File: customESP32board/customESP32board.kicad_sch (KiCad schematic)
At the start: 50 parts, among them J1 USB_B_Micro, J2 Conn_01x16_Pin, J3 Conn_01x16_Pin, Q1 S8050, Q2 S8050, Q3 BSS138, Q4 BSS138, Q5 BSS138, SW1 SW_Push, SW2 SW_Push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

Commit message: update pcb board size to 65mm x 60mm
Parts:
- J1: footprint Connector_USB:USB_Micro-B_Wuerth_629105150521 -> Connector_USB:USB_C_Receptacle_GCT_USB4125-xx-x-0190_6P_TopMnt_Horizontal
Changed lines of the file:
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@@
 			)
 		)
-		(property "Footprint" "Connector_USB:USB_Micro-B_Wuerth_629105150521"
+		(property "Footprint" "Connector_USB:USB_C_Receptacle_GCT_USB4125-xx-x-0190_6P_TopMnt_Horizontal"
 			(at 25.4 41.91 0)
 			(effects

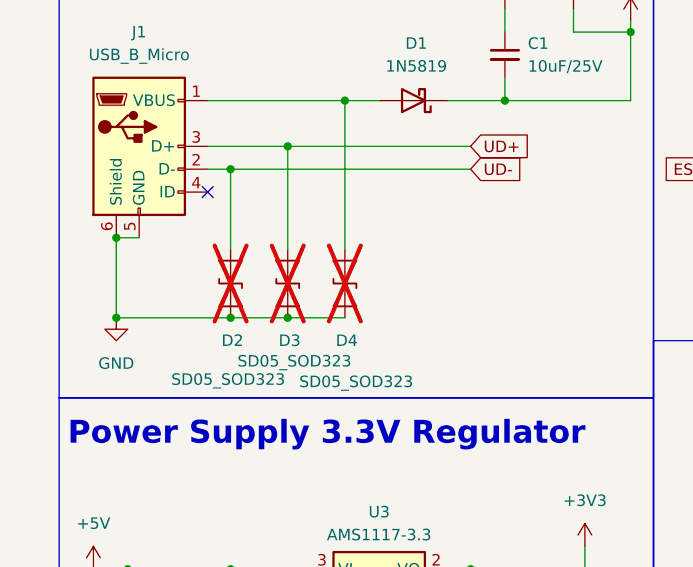
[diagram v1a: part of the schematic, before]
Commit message: updated D+ and D- routing
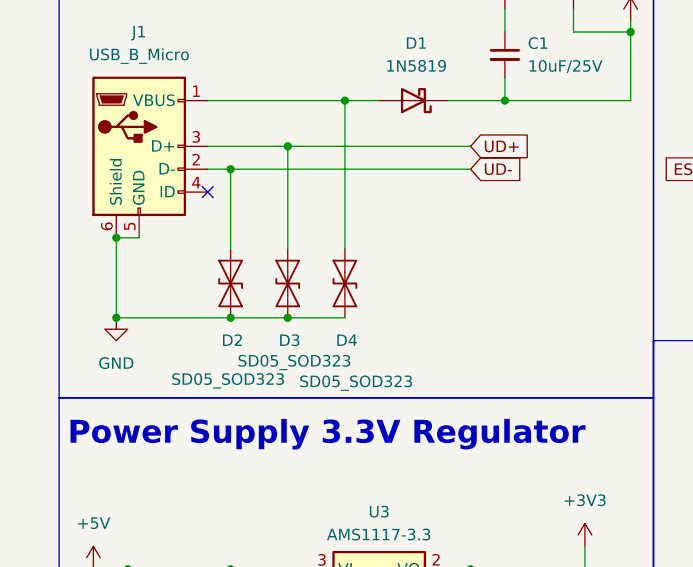
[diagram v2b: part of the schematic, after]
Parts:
- D2, D3, D4: now fitted; now in the parts list
- J1: footprint Connector_USB:USB_C_Receptacle_GCT_USB4125-xx-x-0190_6P_TopMnt_Horizontal -> Connector_USB:USB_Micro-B_Wuerth_629105150521
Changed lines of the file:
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@@
 			)
 		)
-		(property "Footprint" "Connector_USB:USB_C_Receptacle_GCT_USB4125-xx-x-0190_6P_TopMnt_Horizontal"
+		(property "Footprint" "Connector_USB:USB_Micro-B_Wuerth_629105150521"
 			(at 25.4 41.91 0)
 			(effects
@@
 		(unit 1)
 		(exclude_from_sim no)
-		(in_bom no)
-		(on_board no)
-		(dnp yes)
+		(in_bom yes)
+		(on_board yes)
+		(dnp no)
 		(property "Reference" "D4"
 			(at 43.434 62.23 90)
@@
 		(unit 1)
 		(exclude_from_sim no)
-		(in_bom no)
-		(on_board no)
-		(dnp yes)
+		(in_bom yes)
+		(on_board yes)
+		(dnp no)
 		(property "Reference" "D3"
 			(at 37.084 62.23 90)
@@
 		(unit 1)
 		(exclude_from_sim no)
-		(in_bom no)
-		(on_board no)
-		(dnp yes)
+		(in_bom yes)
+		(on_board yes)
+		(dnp no)
 		(property "Reference" "D2"
 			(at 30.734 62.23 90)

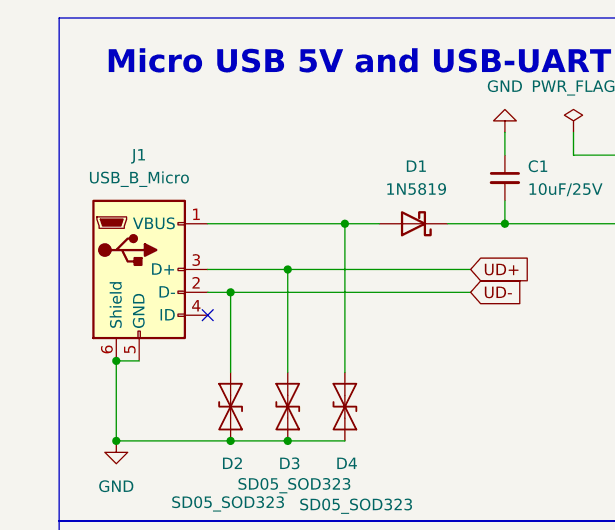
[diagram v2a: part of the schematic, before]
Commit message: updated connector to USB Type B for production DRC constraints
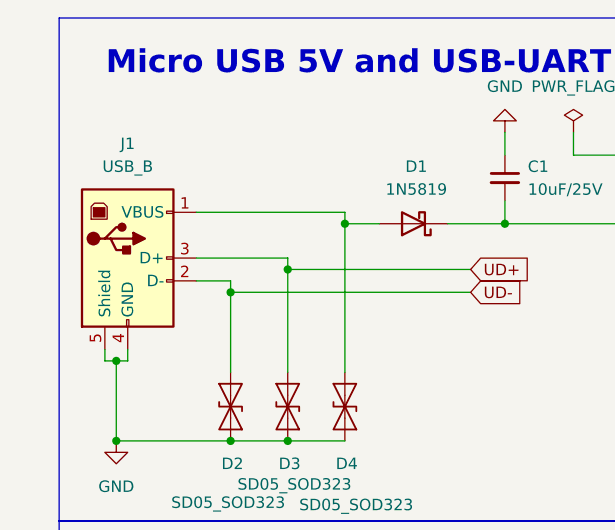
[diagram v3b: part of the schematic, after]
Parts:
- removed J1: USB_B_Micro, Connector_USB:USB_Micro-B_Wuerth_629105150521, symbol Connector:USB_B_Micro
- added J1: USB_B, Connector_USB:USB_B_OST_USB-B1HSxx_Horizontal, symbol Connector:USB_B
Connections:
- net GND: now also J1.4 (GND), J1.5 (Shield)
- net UD+: now also J1.3 (D+)
- net UD-: now also J1.2 (D-)
- net at D1.2 (A), D4.2 (A2): now also J1.1 (VBUS)
- no-connect marks 13 -> 12
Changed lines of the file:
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@@
 	)
 	(junction
-		(at 19.05 50.8)
-		(diameter 0)
-		(color 0 0 0 0)
-	)
-	(junction
 		(at 44.45 35.56)
 		(diameter 0)
@@
 	)
 	(junction
+		(at 19.05 50.8)
+		(diameter 0)
+		(color 0 0 0 0)
+	)
+	(junction
 		(at 76.2 27.94)
 		(diameter 0)
@@
 	)
 	(no_connect
-		(at 29.21 45.72)
-	)
-	(no_connect
 		(at 234.95 69.85)
 	)
@@
 	(wire
 		(pts
-			(xy 31.75 43.18) (xy 29.21 43.18)
+			(xy 31.75 41.91) (xy 27.94 41.91)
 		)
 		(stroke
@@
 	(wire
 		(pts
+			(xy 44.45 34.29) (xy 44.45 35.56)
+		)
+		(stroke
+			(width 0)
+			(type default)
+		)
+	)
+	(wire
+		(pts
 			(xy 20.32 87.63) (xy 31.75 87.63)
 		)
@@
 	(wire
 		(pts
+			(xy 17.78 50.8) (xy 19.05 50.8)
+		)
+		(stroke
+			(width 0)
+			(type default)
+		)
+	)
+	(wire
+		(pts
 			(xy 49.53 134.62) (xy 52.07 134.62)
 		)
@@
 	(wire
 		(pts
+			(xy 17.78 49.53) (xy 17.78 50.8)
+		)
+		(stroke
+			(width 0)
+			(type default)
+		)
+	)
+	(wire
+		(pts
 			(xy 16.51 87.63) (xy 20.32 87.63)
 		)
@@
 	(wire
 		(pts
+			(xy 31.75 41.91) (xy 31.75 43.18)
+		)
+		(stroke
+			(width 0)
+			(type default)
+		)
+	)
+	(wire
+		(pts
 			(xy 88.9 167.64) (xy 88.9 156.21)
 		)
@@
 	(wire
 		(pts
-			(xy 19.05 50.8) (xy 21.59 50.8)
+			(xy 171.45 149.86) (xy 186.69 149.86)
 		)
 		(stroke
@@
 	(wire
 		(pts
-			(xy 171.45 149.86) (xy 186.69 149.86)
+			(xy 20.32 49.53) (xy 20.32 50.8)
+		)
+		(stroke
+			(width 0)
+			(type default)
+		)
+	)
+	(wire
+		(pts
+			(xy 20.32 50.8) (xy 19.05 50.8)
 		)
 		(stroke
@@
 	(wire
 		(pts
-			(xy 29.21 35.56) (xy 44.45 35.56)
+			(xy 27.94 34.29) (xy 44.45 34.29)
 		)
 		(stroke
@@
 	(wire
 		(pts
-			(xy 29.21 40.64) (xy 38.1 40.64)
+			(xy 27.94 39.37) (xy 38.1 39.37)
 		)
 		(stroke
@@
 		)
 	)
+	(wire
+		(pts
+			(xy 38.1 39.37) (xy 38.1 40.64)
+		)
+		(stroke
+			(width 0)
+			(type default)
+		)
+	)
 	(polyline
 		(pts
@@
 	)
 	(symbol
+		(lib_id "Connector:USB_B")
+		(at 20.32 39.37 0)
+		(unit 1)
+		(exclude_from_sim no)
+		(in_bom yes)
+		(on_board yes)
+		(dnp no)
+		(fields_autoplaced yes)
+		(property "Reference" "J1"
+			(at 20.32 26.67 0)
+			(effects
+				(font
+					(size 1.27 1.27)
+				)
+			)
+		)
+		(property "Value" "USB_B"
+			(at 20.32 29.21 0)
+			(effects
+				(font
+					(size 1.27 1.27)
+				)
+			)
+		)
+		(property "Footprint" "Connector_USB:USB_B_OST_USB-B1HSxx_Horizontal"
+			(at 24.13 40.64 0)
+			(effects
+				(font
+					(size 1.27 1.27)
+				)
+				(hide yes)
+			)
+		)
+		(property "Datasheet" "https://makerselectronics.com/product/usb-connector-on-pcb-b-type-female/?srsltid=AfmBOor0KxhBgwTNPC40mW2aFZHyVsxA8Kw2CJfDPEyBWQGF0YMEHq_R"
+			(at 24.13 40.64 0)
+			(effects
+				(font
+					(size 1.27 1.27)
+				)
+				(hide yes)
+			)
+		)
+		(property "Description" "USB Type B connector"
+			(at 20.32 39.37 0)
+			(effects
+				(font
+					(size 1.27 1.27)
+				)
+				(hide yes)
+			)
+		)
+		(property "link" "https://makerselectronics.com/product/usb-connector-on-pcb-b-type-female/?srsltid=AfmBOor0KxhBgwTNPC40mW2aFZHyVsxA8Kw2CJfDPEyBWQGF0YMEHq_R"
+			(at 20.32 39.37 0)
+			(effects
+				(font
+					(size 1.27 1.27)
+				)
+				(hide yes)
+			)
+		)
+		(pin "5"
+		)
+		(pin "1"
+		)
+		(pin "4"
+		)
+		(pin "3"
+		)
+		(pin "2"
+		)
+		(instances
+			(project ""
+				(path "/cd0f6669-7f9d-4241-9b3e-05618ad516f1"
+					(reference "J1")
+					(unit 1)
+				)
+			)
+		)
+	)
+	(symbol
 		(lib_id "Device:C_Polarized")
 		(at 58.42 91.44 0)
@@
 					(unit 1)
 				)
-			)
-		)
-	)
-	(symbol
-		(lib_id "Connector:USB_B_Micro")
-		(at 21.59 40.64 0)
-		(unit 1)
-		(exclude_from_sim no)
-		(in_bom yes)
-		(on_board yes)
-		(dnp no)
-		(fields_autoplaced yes)
-		(property "Reference" "J1"
-			(at 21.59 27.94 0)
-			(effects
-				(font
-					(size 1.27 1.27)
-				)
-			)
-		)
-		(property "Value" "USB_B_Micro"
-			(at 21.59 30.48 0)
-			(effects
-				(font
-					(size 1.27 1.27)
-				)
-			)
-		)
-		(property "Footprint" "Connector_USB:USB_Micro-B_Wuerth_629105150521"
-			(at 25.4 41.91 0)
-			(effects
-				(font
-					(size 1.27 1.27)
-				)
-				(hide yes)
-			)
-		)
-		(property "Datasheet" "https://uge-one.com/product/micro-usb-5pin-smd-connector-4-legs/?srsltid=AfmBOooYsLu83HBX0h_ZTWFs7ijfYeXHbH9weshkzWBaOrYEr-u_RTRQ"
-			(at 25.4 41.91 0)
-			(effects
-				(font
-					(size 1.27 1.27)
-				)
-				(hide yes)
-			)
-		)
-		(property "Description" "USB Micro Type B connector"
-			(at 21.59 40.64 0)
-			(effects
-				(font
-					(size 1.27 1.27)
-				)
-				(hide yes)
-			)
-		)
-		(property "link" "https://uge-one.com/product/micro-usb-5pin-smd-connector-4-legs/?srsltid=AfmBOooYsLu83HBX0h_ZTWFs7ijfYeXHbH9weshkzWBaOrYEr-u_RTRQ"
-			(at 21.59 40.64 0)
-			(effects
-				(font
-					(size 1.27 1.27)
-				)
-				(hide yes)
-			)
-		)
-		(pin "1"
-		)
-		(pin "5"
-		)
-		(pin "2"
-		)
-		(pin "4"
-		)
-		(pin "6"
-		)
-		(pin "3"
-		)
-		(instances
-			(project ""
-				(path "/cd0f6669-7f9d-4241-9b3e-05618ad516f1"
-					(reference "J1")
-					(unit 1)
-				)

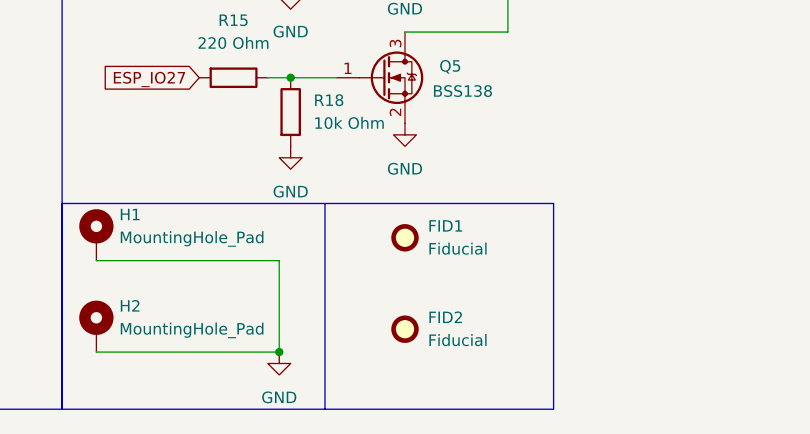
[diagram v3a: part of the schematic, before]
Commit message: updated routing, placemennt, new USB B footprint
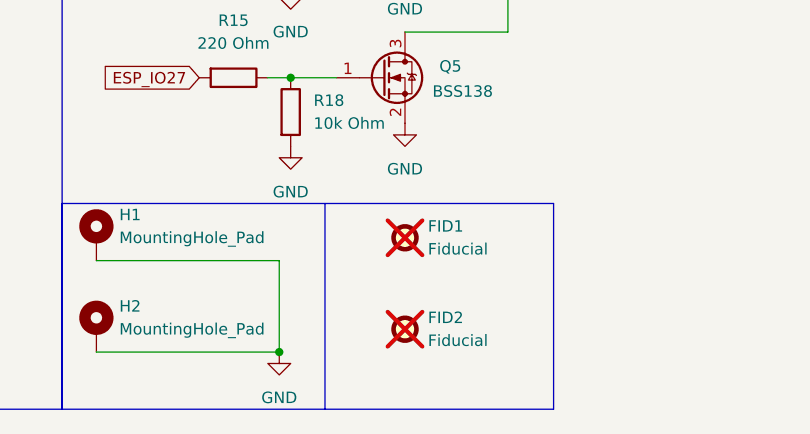
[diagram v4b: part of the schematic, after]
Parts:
- FID1, FID2: now not fitted
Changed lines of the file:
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@@
 		(exclude_from_sim no)
 		(in_bom no)
-		(on_board yes)
-		(dnp no)
+		(on_board no)
+		(dnp yes)
 		(fields_autoplaced yes)
 		(property "Reference" "FID2"
@@
 		(exclude_from_sim no)
 		(in_bom no)
-		(on_board yes)
-		(dnp no)
+		(on_board no)
+		(dnp yes)
 		(fields_autoplaced yes)
 		(property "Reference" "FID1"

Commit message: updated components list and updated BOM and calculated price list
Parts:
- SW1: link https://uge-one.com/product/smd-micro-push-button-switch-2p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 -> https://uge-one.com/product/smd-micro-switch-white-tact-s-3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
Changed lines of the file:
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@@
 			)
 		)
-		(property "link" "https://uge-one.com/product/smd-micro-push-button-switch-2p-3x4x2mm/"
+		(property "link" "https://uge-one.com/product/smd-micro-switch-white-tact-s-3-6-5-2-pin/"
 			(at 91.44 48.26 90)
 			(effects

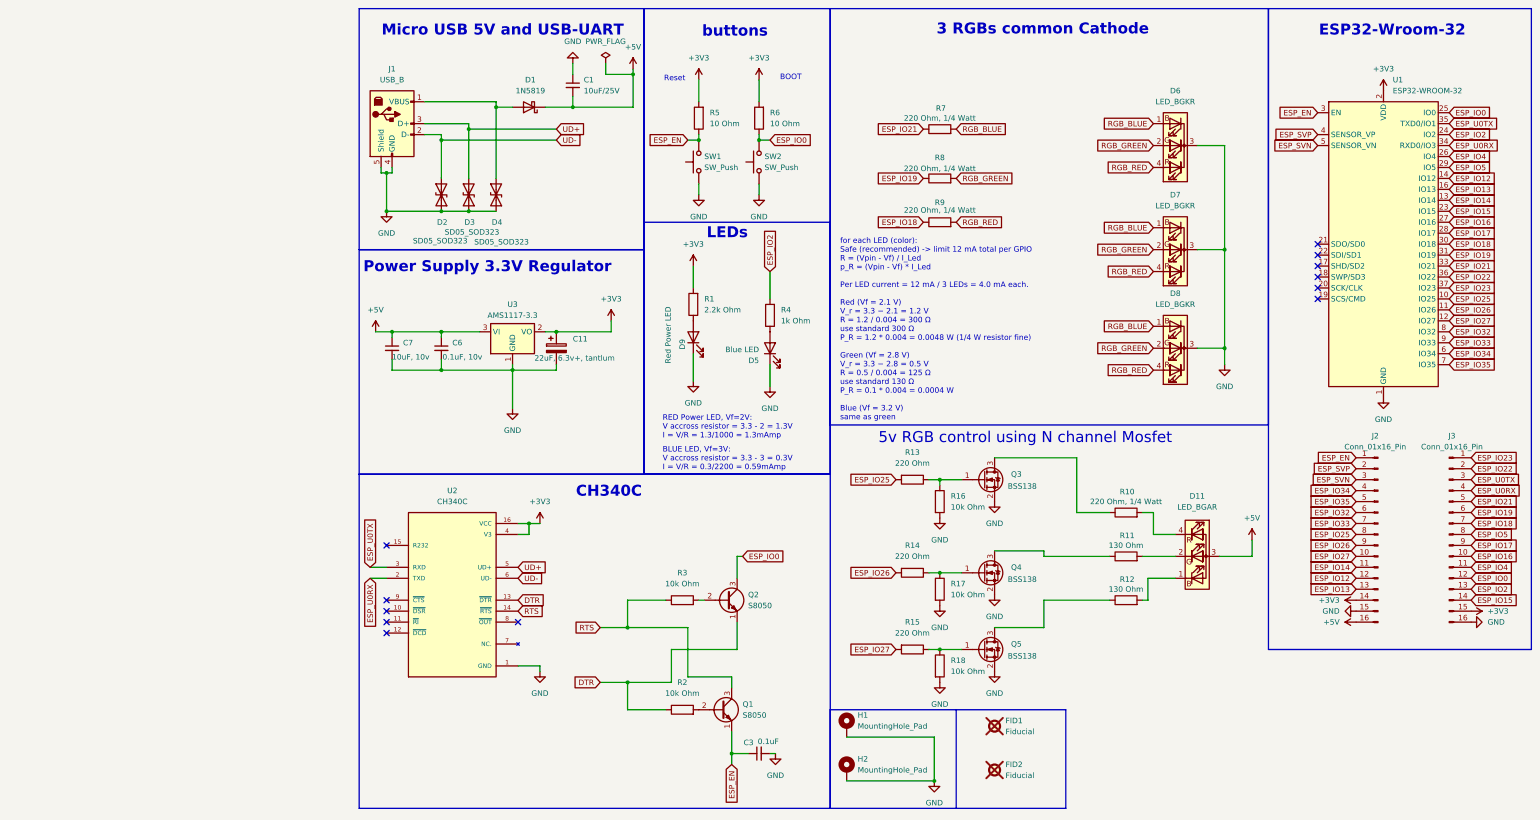
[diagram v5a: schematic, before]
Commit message: generated BOM again, finished price list and ordered it
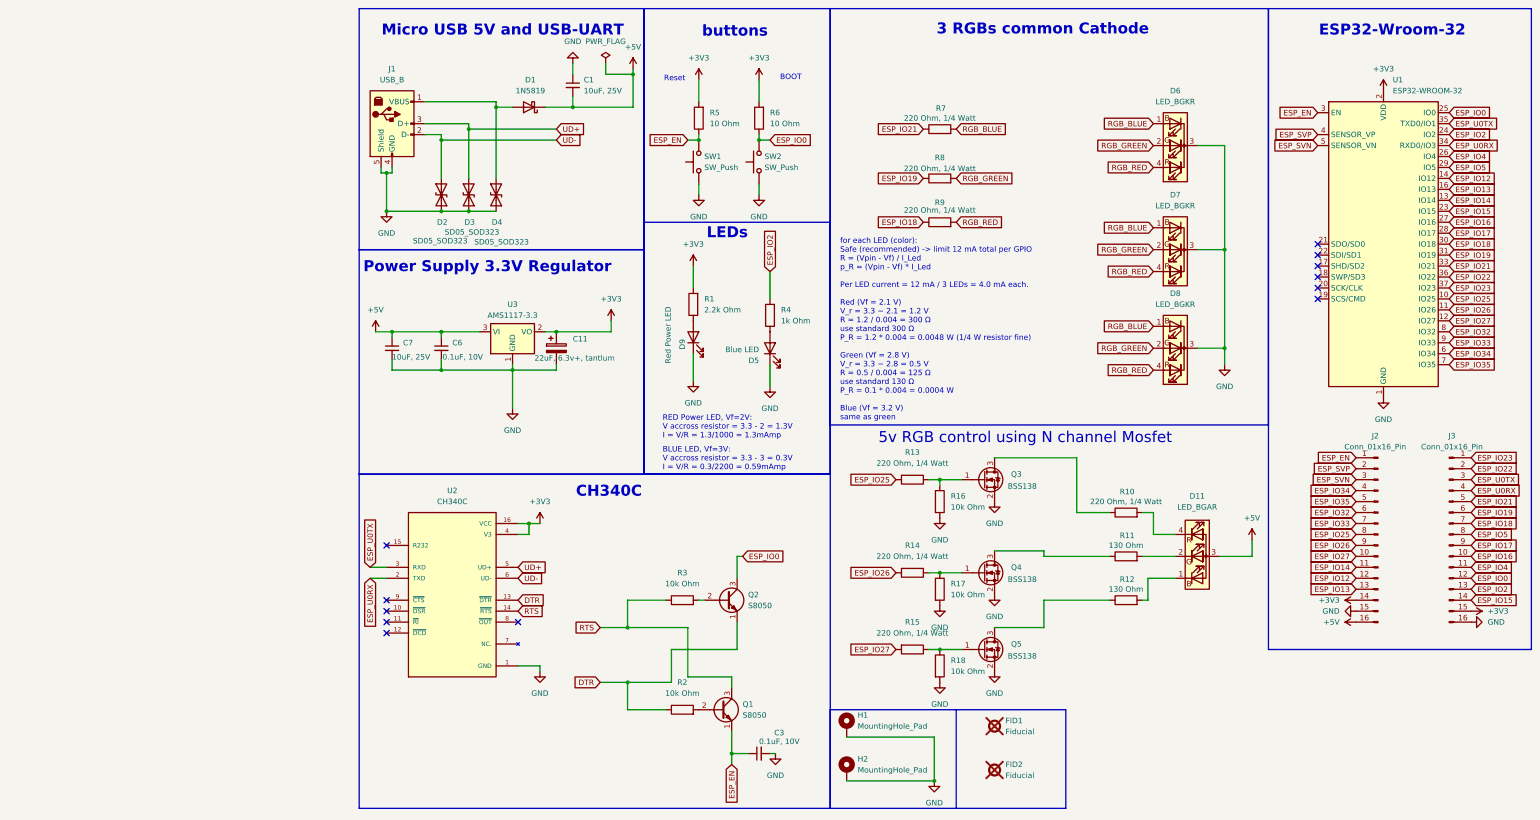
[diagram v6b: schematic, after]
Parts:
- C1: value 10uF/25V -> 10uF, 25V
- C3: value 0.1uF -> 0.1uF, 10V
- C6: value 0.1uF, 10v -> 0.1uF, 10V
- C7: value 10uF, 10v -> 10uF, 25V
- R13, R14, R15: value 220 Ohm -> 220 Ohm, 1/4 Watt
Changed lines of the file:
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@@
 			)
 		)
-		(property "Value" "220 Ohm"
+		(property "Value" "220 Ohm, 1/4 Watt"
 			(at 140.97 118.11 90)
 			(effects
@@
 			)
 		)
-		(property "Value" "10uF/25V"
+		(property "Value" "10uF, 25V"
 			(at 64.77 31.7562 0)
 			(effects
@@
 			)
 		)
-		(property "Value" "0.1uF, 10v"
+		(property "Value" "0.1uF, 10V"
 			(at 32.004 93.472 0)
 			(effects
@@
 			)
 		)
-		(property "Value" "10uF, 10v"
+		(property "Value" "10uF, 25V"
 			(at 20.32 93.472 0)
 			(effects
@@
 			)
 		)
-		(property "Value" "220 Ohm"
+		(property "Value" "220 Ohm, 1/4 Watt"
 			(at 140.97 139.7 90)
 			(effects
@@
 		(dnp no)
 		(property "Reference" "C3"
-			(at 104.1462 182.88 90)
+			(at 111.252 180.594 90)
 			(effects
 				(font
@@
 			)
 		)
-		(property "Value" "0.1uF"
-			(at 109.982 182.626 90)
+		(property "Value" "0.1uF, 10V"
+			(at 114.808 182.626 90)
 			(effects
 				(font
@@
 			)
 		)
-		(property "Value" "220 Ohm"
+		(property "Value" "220 Ohm, 1/4 Watt"
 			(at 140.97 157.48 90)
 			(effects
